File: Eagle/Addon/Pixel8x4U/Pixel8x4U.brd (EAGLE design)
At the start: 52.4 x 55.9 mm, 28 parts, among them J1 5V, J2 I2C, J3 RJ45, J4 RJ45, J5 GPIOC, Q1 DIODES_INC._DMG2305UX-13DIODE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, Q2 DMMT5401-7-F_0_0, U1 74HCT245

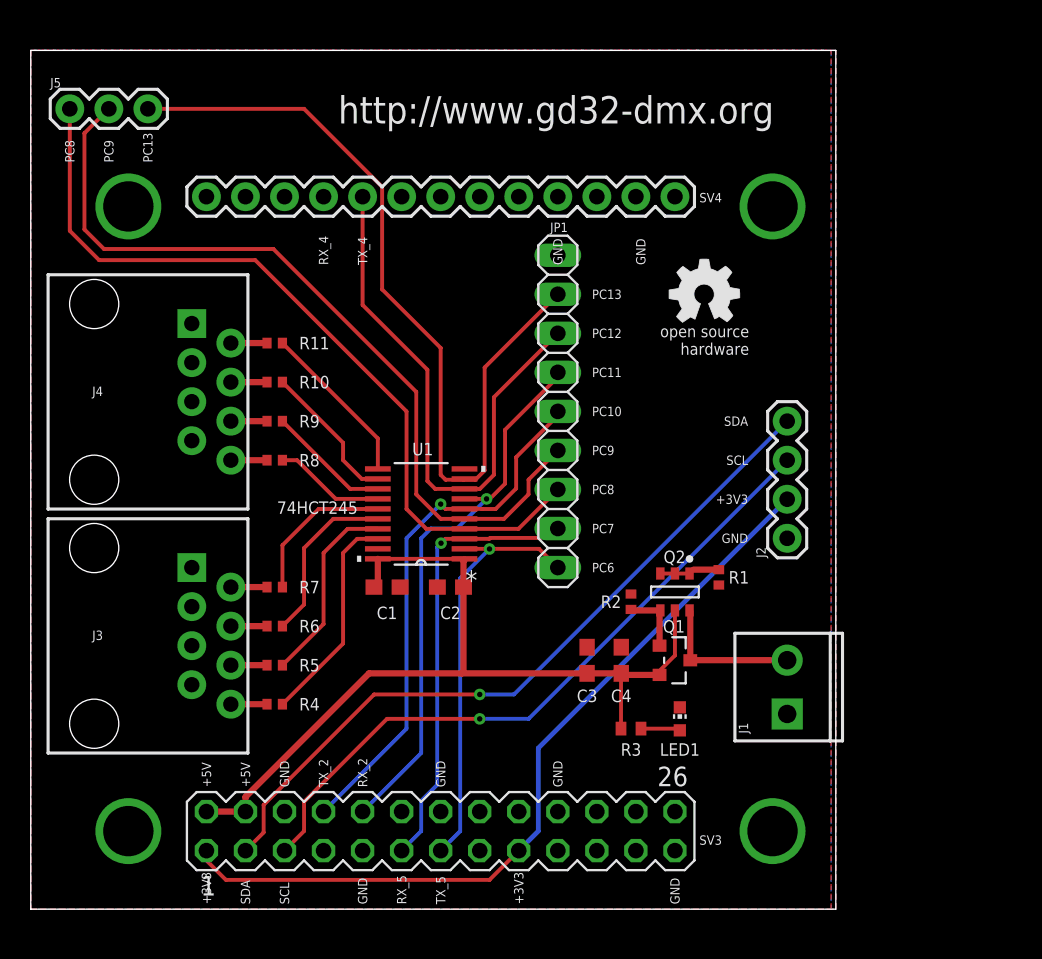
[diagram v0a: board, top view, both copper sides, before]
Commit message: Updated Add-on Pixel 8x 4 Universes
*. Added support for clock based led chip's (for example APA102)
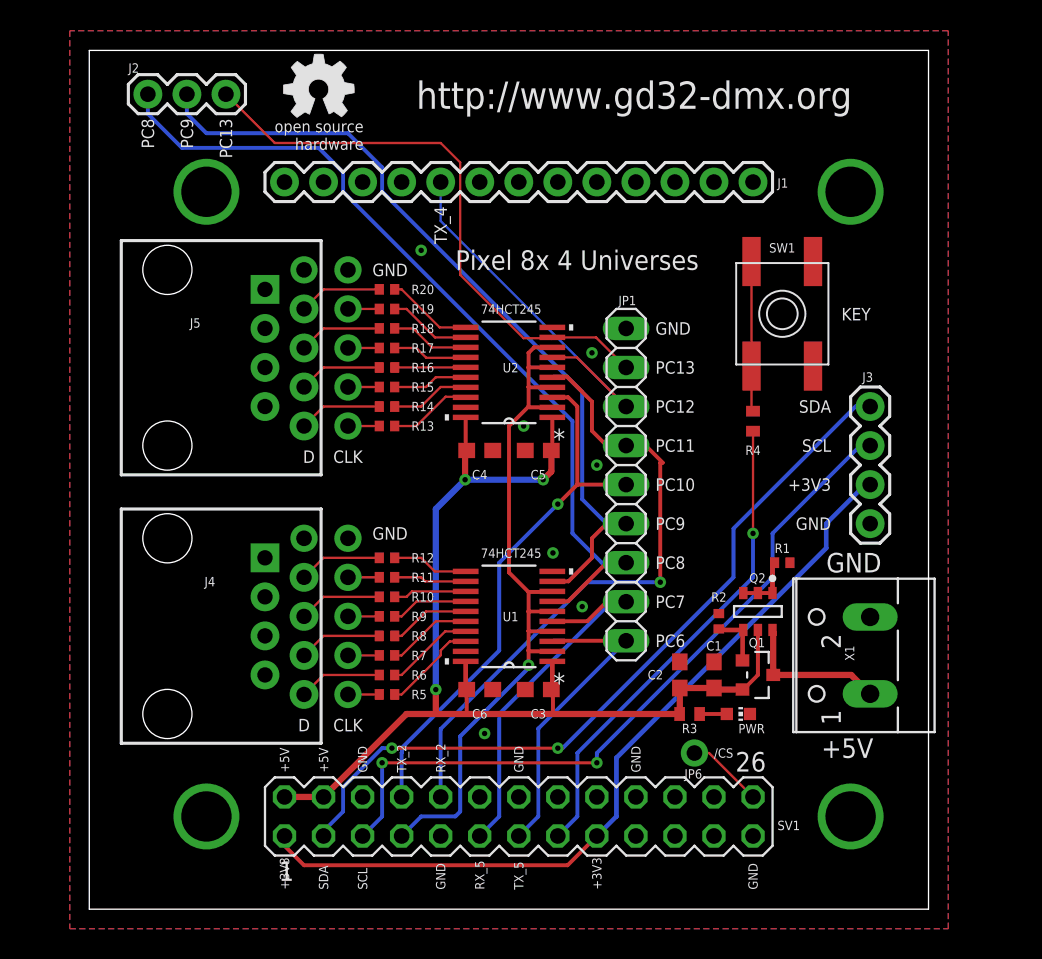
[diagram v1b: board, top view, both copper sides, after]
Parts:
- removed SV3: GPIO, con-lstb:MA13-2
- removed SV4: GPIO, SparkFun-Connectors:1X13
- added C5, C6: 100n, rcl:C0603
- added CN1: CLOCK-1-4, adafruit:1X04-CLEANBIG
- added CN2: CLOCK-5-8, adafruit:1X04-CLEANBIG
- added JP2, JP3, JP4, JP5: GND, adafruit:1X01-CLEANBIG
- added JP6: /CS, adafruit:1X01-CLEANBIG
- added R12, R13, R14, R15, R16, R17, R18, R19, R20: 100, rcl:R0402
- added SV1: GPIO, con-lstb:MA13-2
- added SW1: KEY, adafruit:EVQ-Q2
- added U2: 74HCT245, SN74HCT245PWR:PW20
- added X1: (no value), con-wago-500:W237-102
- J1: value 5V -> GPIO; device SparkFun-Connectors:SCREWTERMINAL-3.5MM-2 -> SparkFun-Connectors:1X13
- J2: value I2C -> GPIOC; device SparkFun-Connectors:1X04 -> SparkFun-Connectors:1X03
- J3: value RJ45 -> I2C; device SparkFun-Connectors:RJ45-8 -> SparkFun-Connectors:1X04
- J5: value GPIOC -> RJ45; device SparkFun-Connectors:1X03 -> SparkFun-Connectors:RJ45-8
- JP1: value (none) -> DEBUG
- R4: value 100 -> 1K; device rcl:R0402 -> resistor:R0402
- moved J3 51.0 mm to (54.6, 25.1), turned to 90 degrees
- moved J2 50.6 mm to (7.62, 53.0), turned to 0 degrees
- moved R4 36.2 mm to (47.0, 31.8), turned to 270 degrees
- moved J1 34.7 mm to (47.0, 47.3), turned to 180 degrees
- moved GOLD_ORB_SM1 28.4 mm to (18.7, 53.3)
- moved C1 22.0 mm to (44.5, 15.2), turned to 90 degrees
- moved J5 17.4 mm to (8.89, 35.9), turned to 270 degrees
- moved R11 16.9 mm to (23.2, 21.6)
- moved C4 16.5 mm to (29.2, 29.8), turned to 0 degrees
- moved C2 16.0 mm to (42.2, 15.2), turned to 90 degrees
- moved J4 16.0 mm to (8.89, 18.4)
- moved R10 15.8 mm to (23.2, 20.3)
- moved R9 14.6 mm to (23.2, 19.1)
- moved R8 13.6 mm to (23.2, 17.8)
- moved U1 8.78 mm to (31.1, 19.1)
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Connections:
- removed net B1: R4.1, U1.18
- removed net B2: R5.1, U1.17
- removed net B3: R6.1, U1.16
- removed net B4: R7.1, U1.15
- removed net B5: R8.1, U1.14
- removed net B6: R9.1, U1.13
- removed net B7: R10.1, U1.12
- removed net B8: R11.1, U1.11
- new net C1: CN1.1, R5.2
- new net C2: CN1.2, R7.2
- new net C3: CN1.3, R9.2
- new net C4: CN1.4, R11.2
- new net C5: CN2.1, R13.2
- new net C6: CN2.2, R15.2
- new net C7: CN2.3, R17.2
- new net C8: CN2.4, R19.2
- new net N$10: R7.1, U1.16
- new net N$11: R14.1, U2.17
- new net N$12: R16.1, U2.15
- new net N$13: R18.1, U2.13
- new net N$15: R20.1, U2.11
- new net N$16: R9.1, U1.14
- new net N$17: R11.1, U1.12
- new net N$18: R13.1, U2.18
- new net N$19: R15.1, U2.16
- new net N$20: R17.1, U2.14
- new net N$21: R19.1, U2.12
- new net N$4: R4.1, SW1.B, SW1.B'
- new net N$5: R6.1, U1.17
- new net N$6: R12.1, U1.11
- new net N$7: R10.1, U1.13
- new net N$8: R8.1, U1.15
- new net N$9: R5.1, U1.18
- new net PA14: JP6.1, SV1.26
- new net PA6: SV1.7, U1.2, U1.4, U1.6, U1.8, U2.2, U2.4, U2.6, U2.8
- new net PB14: R4.2, SV1.15
- net +3V3: now also J3.2, SV1.1, SV1.17; no longer J2.2, SV3.1, SV3.17
- net +5V: now also C5.1, C6.1, SV1.2, SV1.4, U2.1, U2.20; no longer SV3.2, SV3.4
- net GND: now also C5.2, C6.2, J1.13, J1.2, J1.4, J5.1, J5.3, J5.5, J5.7, JP2.1, JP3.1, JP4.1, JP5.1, SV1.14, SV1.20, SV1.25, SV1.6, SV1.9, SW1.A, SW1.A', U2.10, U2.19, X1.2; no longer J1.1, J2.1, J3.3, J3.5, J3.7, SV3.14, SV3.20, SV3.25, SV3.6, SV3.9, SV4.13, SV4.2, SV4.4
- net I2C0_SCL: now also J3.3, SV1.5; no longer J2.3, SV3.5
- net I2C0_SDA: now also J3.4, SV1.3; no longer J2.4, SV3.3
- net N$2: now also X1.1; no longer J1.2
- net O1: now also J4.8, R6.2; no longer J3.8, R4.2
- net O2: now also J4.6, R8.2; no longer J3.6, R5.2
- net O3: now also J4.4, R10.2; no longer J3.4, R6.2
- net O4: now also J4.2, R12.2; no longer J3.2, R7.2
- net O5: now also J5.8, R14.2; no longer J4.8, R8.2
- net O6: now also J5.6, R16.2; no longer J4.6, R9.2
- net O7: now also J5.4, R18.2; no longer J4.4, R10.2
- net O8: now also J5.2, R20.2; no longer J4.2, R11.2
- net PC13: now also J2.3, U2.9; no longer J5.3, U1.9
- net PC8: now also J2.1, U1.7; no longer J5.1, U1.4
- net PC9: now also J2.2, U1.9; no longer J5.2, U1.5
- net UART4_RX: now also J1.10; no longer SV4.10
- net UART4_TX: now also J1.9, U2.7; no longer SV4.9, U1.8
- net USART0_RX: now also J1.12; no longer SV4.12
- net USART0_TX: now also J1.11; no longer SV4.11
- net USART2_RX: now also SV1.10, U2.5; no longer SV3.10, U1.7
- net USART2_TX: now also SV1.8, U2.3; no longer SV3.8, U1.6
- net USART5_RX: now also SV1.11, U1.5; no longer SV3.11, U1.3
- net USART5_TX: now also SV1.13, U1.3; no longer SV3.13, U1.2
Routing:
- net PA6: track 0.00 -> 49.8 mm, vias 0 -> 1
- net PB14: track 0.00 -> 31.6 mm, vias 0 -> 1
- net +5V: track 57.1 -> 74.6 mm, vias 0 -> 3
- net PC13: track 54.4 -> 37.7 mm
- net B1: track 14.1 -> 0.00 mm
- net B2: track 12.6 -> 0.00 mm
- net B3: track 11.2 -> 0.00 mm
- net B8: track 10.8 -> 0.00 mm
- net UART4_TX: track 36.1 -> 25.7 mm
- net B4: track 9.91 -> 0.00 mm
- net N$4: track 0.00 -> 9.77 mm
- net B7: track 9.48 -> 0.00 mm
- net B6: track 8.03 -> 0.00 mm
- net B5: track 7.25 -> 0.00 mm
- net USART5_TX: track 27.5 -> 20.4 mm, vias 1 -> 0
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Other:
- board size 52.4 x 55.9 mm -> 54.6 x 55.9 mm
- board text added: "CLK"
- board text added: "D"
- board text added: "Pixel 8x 4 Universes"
- board text removed: "RX_4"
